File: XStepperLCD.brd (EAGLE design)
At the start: 78.7 x 38.1 mm, 40 parts, among them U1 LCD-16X2NOHOLES, X1 RJ45-6L-B

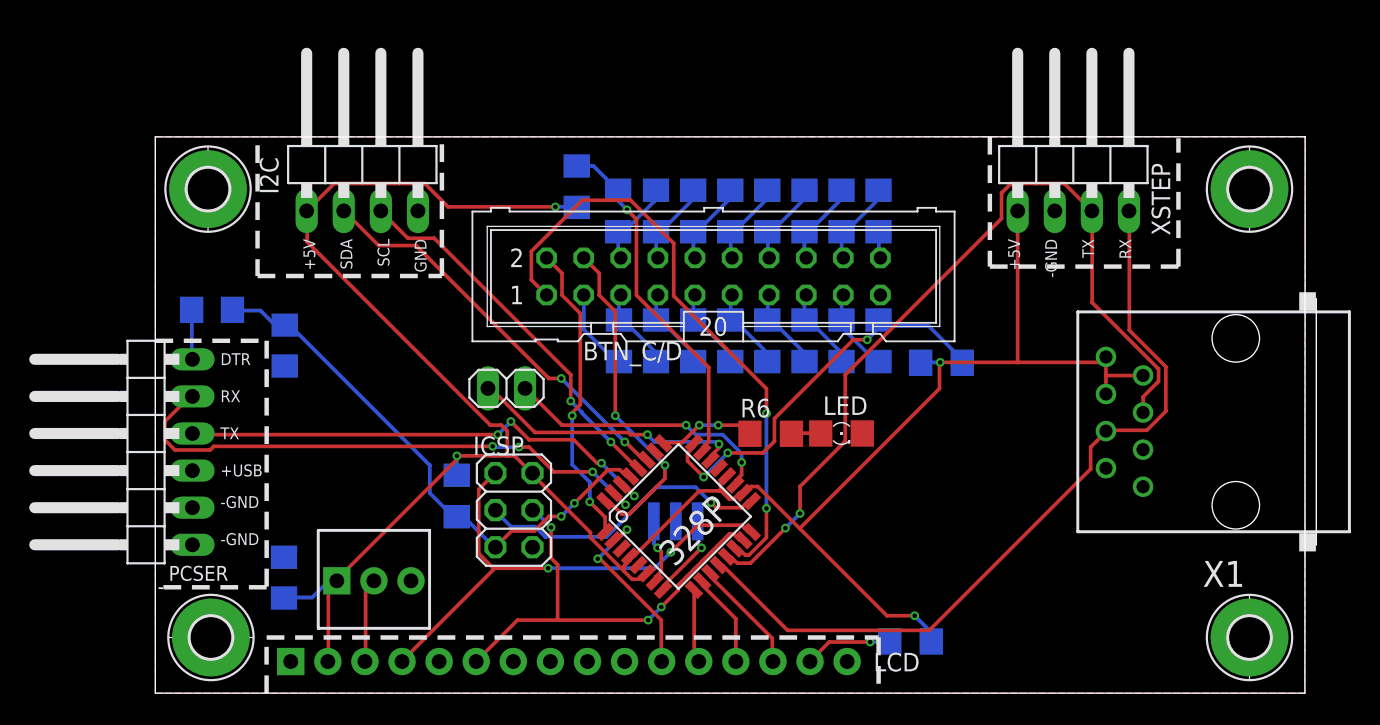
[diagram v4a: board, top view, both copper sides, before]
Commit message: finish to produce
Route new and set some via's.
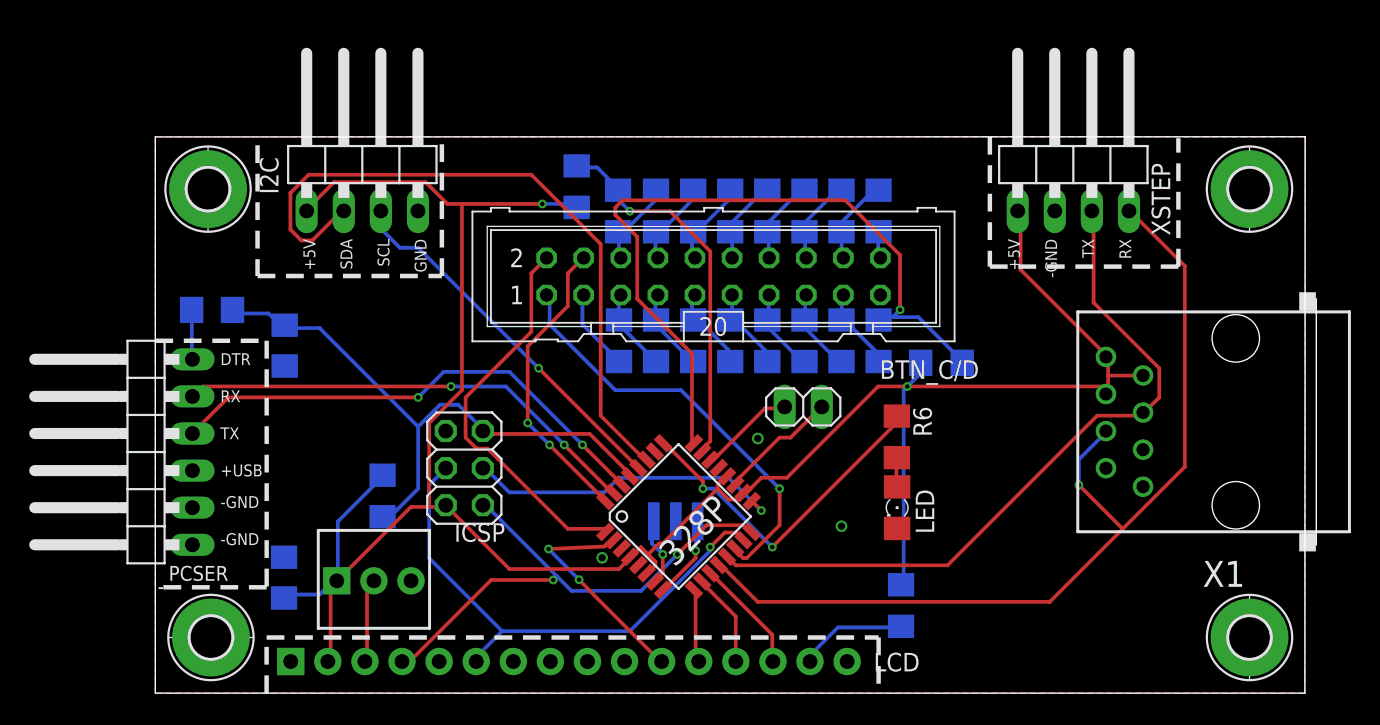
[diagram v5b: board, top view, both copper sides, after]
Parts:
- moved BTN_C/D 20.4 mm to (44.4, 19.6)
- moved R6 8.64 mm to (50.8, 17.6), turned to 270 degrees
- moved LED 6.35 mm to (50.8, 12.7), turned to 270 degrees
- moved R3 5.08 mm to (15.6, 13.5)
- moved ICSP 4.46 mm to (21.2, 15.4), turned to 90 degrees
- moved R2 2.54 mm to (51.1, 6.00), turned to 270 degrees
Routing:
- net BUTTONS_B: track 27.9 -> 51.3 mm, vias 3 -> 1
- net SDA: track 27.8 -> 47.2 mm, vias 2 -> 0
- net N$15: track 6.72 -> 23.4 mm
- net BUTTONS_D: track 18.7 -> 6.58 mm, vias 2 -> 0
- net POT_SELECT: track 41.4 -> 29.4 mm, vias 2 -> 1
- net BUTTONS_C: track 19.0 -> 8.21 mm, vias 2 -> 0
- net RX: track 54.4 -> 64.6 mm, vias 0 -> 1
- net TX: track 57.6 -> 49.4 mm, vias 2 -> 0
- net USB_RXD: track 38.6 -> 32.1 mm, vias 4 -> 2
- net POT_B: track 20.9 -> 26.9 mm, vias 2 -> 0
- net ENABLE/MOSI: track 30.6 -> 36.5 mm, vias 3 -> 1
- net RESET: track 37.5 -> 41.2 mm, vias 2 -> 0
- net VCC: track 156.9 -> 160.4 mm, vias 4 -> 2
- net D4: track 13.0 -> 15.5 mm
- net POT_A: track 22.9 -> 20.4 mm
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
